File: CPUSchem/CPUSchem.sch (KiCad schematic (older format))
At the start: 30 parts

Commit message: Split CPU fetch stage into 2 stages to account for new interconnect
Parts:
- removed U?: IF_ID, symbol SOC:IF_ID
- added U?: IF1_IF2, symbol CPUSchem:IF1_IF2
- added U?: IF2_ID, symbol CPUSchem:IF2_ID
- U? (x10): symbol SOC:2-1Mux -> CPUSchem:2-1Mux
- U?: symbol SOC:MEM_WB -> CPUSchem:MEM_WB
- U?: symbol SOC:LOAD_UPPER -> CPUSchem:LOAD_UPPER
- U?: symbol SOC:3-1MUX -> CPUSchem:3-1MUX
- U? (x3): symbol SOC:ADDER -> CPUSchem:ADDER
- U?: symbol SOC:ID_IE -> CPUSchem:ID_IE
- U?: symbol SOC:IE_MEM -> CPUSchem:IE_MEM
- U?: symbol SOC:REGFILE -> CPUSchem:REGFILE
- U?: symbol SOC:IMM_GEN -> CPUSchem:IMM_GEN
- U?: symbol SOC:PC -> CPUSchem:PC
- U?: symbol SOC:DECODER -> CPUSchem:DECODER
- U?: symbol SOC:BRANCH_UNIT -> CPUSchem:BRANCH_UNIT
- U?: symbol SOC:HAZARD_UNIT -> CPUSchem:HAZARD_UNIT
- U?: symbol SOC:ALU -> CPUSchem:ALU
- U?: symbol SOC:DBUS_MASTER -> CPUSchem:DBUS_MASTER
- U?: symbol SOC:0Comparator -> CPUSchem:0Comparator
- U?: symbol SOC:FORWARDING_UNIT -> CPUSchem:FORWARDING_UNIT
- U?: symbol SOC:IBUS -> CPUSchem:IBUS
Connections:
- net labels added: Clr_F2, DBus_WaitReq_M, En_F2
- net labels removed: DBUS_WaitReq_M
- wire segments 135 -> 136
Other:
- note added: "Two Stage\nPipelined"

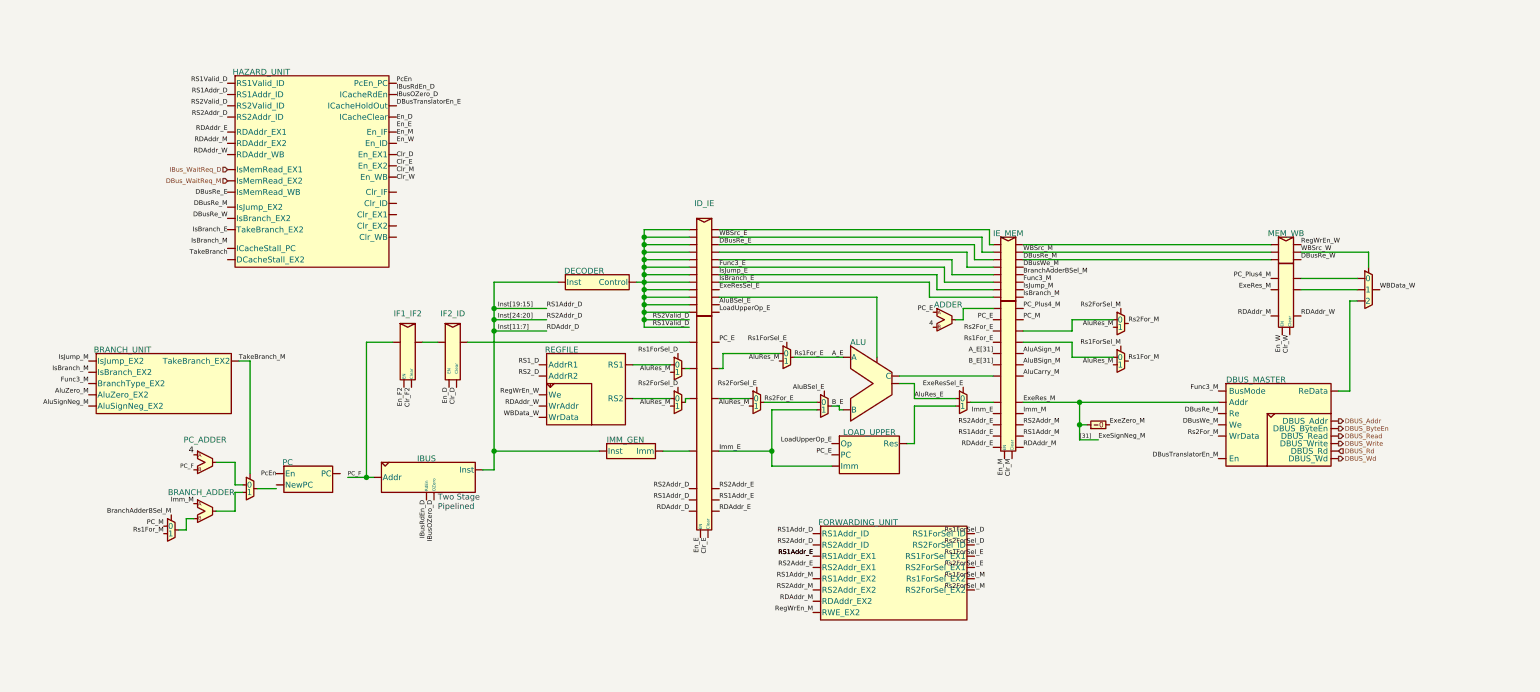
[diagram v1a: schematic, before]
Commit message: More CPU hazzard testing/fixes and verification
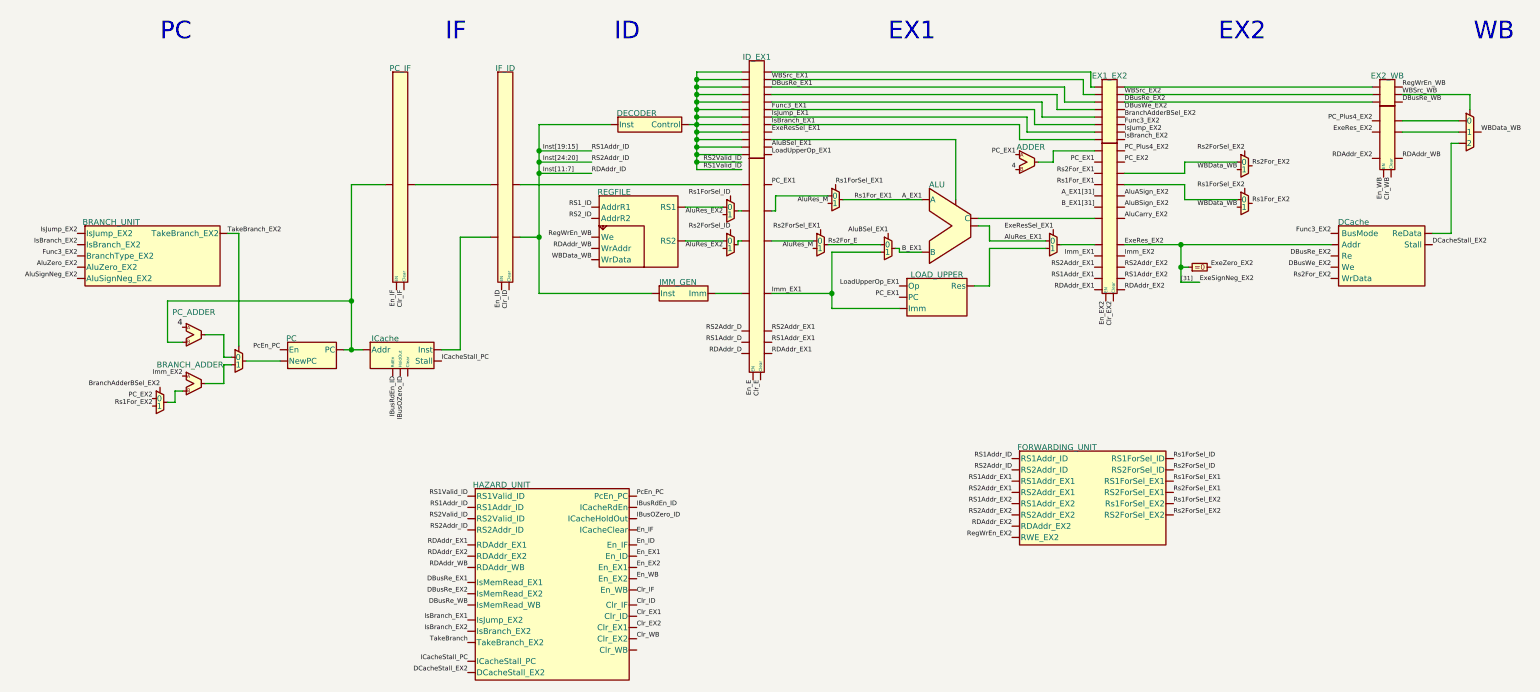
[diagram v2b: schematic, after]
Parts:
- removed U?: MEM_WB, symbol CPUSchem:MEM_WB
- removed U?: ID_IE, symbol CPUSchem:ID_IE
- removed U?: IE_MEM, symbol CPUSchem:IE_MEM
- removed U?: DBUS_MASTER, symbol CPUSchem:DBUS_MASTER
- removed U?: IBUS, symbol CPUSchem:IBUS
- removed U?: IF1_IF2, symbol CPUSchem:IF1_IF2
- removed U?: IF2_ID, symbol CPUSchem:IF2_ID
- added U?: PC_IF, symbol CPUSchem:PC_IF
- added U?: ICache, symbol CPUSchem:ICache
- added U?: IF_ID, symbol CPUSchem:IF_ID
- added U?: ID_EX1, symbol CPUSchem:ID_EX1
- added U?: EX1_EX2, symbol CPUSchem:EX1_EX2
- added U?: DCache, symbol CPUSchem:DCache
- added U?: EX2_WB, symbol CPUSchem:EX2_WB
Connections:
- net AluBSel_E is gone; now on net Rs2For_E: U?.~
- net AluSignNeg_M is gone; now on net TakeBranch_EX2: U?.~ (TakeBranch_EX2)
- net AluZero_M is gone; now on net TakeBranch_EX2: U?.~ (TakeBranch_EX2)
- net BranchAdderBSel_M is gone; now on net Rs1For_EX2: U?.~
- net DBusRe_M is gone; now on net TakeBranch: U?.~ (TakeBranch_EX2)
- net DBusRe_W is gone; now on net TakeBranch: U?.~ (TakeBranch_EX2)
- net DBusTranslatorEn_E is gone; now on net TakeBranch: U?.~ (TakeBranch_EX2)
- net DBus_WaitReq_M is gone; now on net TakeBranch: U?.~ (TakeBranch_EX2)
- net En_W is gone; now on net TakeBranch: U?.~ (TakeBranch_EX2)
- net ExeResSel_E is gone; now on net ExeResSel_EX1: U?.~
- net ExeZero_M is gone; now on net ExeZero_EX2: U?.~
- net Func3_M is gone; now on net TakeBranch_EX2: U?.~ (TakeBranch_EX2)
- net IBus_WaitReq_D is gone; now on net TakeBranch: U?.~ (TakeBranch_EX2)
- net Imm_M is gone; now on net Imm_EX2: U?.~
- net IsBranch_M is gone; now on net TakeBranch_EX2: U?.~ (TakeBranch_EX2)
- net IsJump_M is gone; now on net TakeBranch_EX2: U?.~ (TakeBranch_EX2)
- net LoadUpperOp_E is gone; now on net PC_EX1: U?.~ (Res)
- net PC_E is gone; now on net PC_EX1: U?.~, U?.~ (Res)
- net PC_F is gone; now on net 4: U?.~
- net PC_M is gone; now on net Rs1For_EX2: U?.~
- net PcEn is gone; now on net TakeBranch: U?.~ (TakeBranch_EX2)
- net RDAddr_E is gone; now on net TakeBranch: U?.~ (TakeBranch_EX2)
- net RS1Addr_E is gone; now on net Rs2ForSel_ID: U?.~ (RWE_EX2)
- net RS1Addr_M is gone; now on net Rs2ForSel_ID: U?.~ (RWE_EX2)
- net RS1_D is gone; now on net WBData_WB: U?.~ (WrData)
- net RS2Addr_E is gone; now on net Rs2ForSel_ID: U?.~ (RWE_EX2)
- net RS2Addr_M is gone; now on net Rs2ForSel_ID: U?.~ (RWE_EX2)
- net RS2_D is gone; now on net WBData_WB: U?.~ (WrData)
- net RegWrEn_M is gone; now on net Rs2ForSel_ID: U?.~ (RWE_EX2)
- net RegWrEn_W is gone; now on net WBData_WB: U?.~ (WrData)
- net Rs1ForSel_D is gone; now on net Rs1ForSel_ID: U?.~
- net Rs1ForSel_E is gone; now on net Rs1ForSel_EX1: U?.~
- net Rs1ForSel_M is gone; now on net WBData_WB: U?.~
- net Rs2ForSel_D is gone; now on net Rs2ForSel_ID: U?.~
- net Rs2ForSel_E is gone; now on net Rs2For_E: U?.~
- net Rs2ForSel_M is gone; now on net WBData_WB: U?.~
- net Rs2For_M is gone; now on net WBData_WB: U?.~
- net TakeBranch_M is gone; now on net TakeBranch_EX2: U?.~, U?.~ (TakeBranch_EX2)
- net WBSrc_W is gone; now on net WBSrc_WB: U?.~
- net AluRes_M: no longer U?.~, U?.~, U?.~, U?.~
- net Clr_E: now also U?.~; no longer U?.~ (TakeBranch_EX2)
- net En_E: now also U?.~
- net Inst[11:7]: now also U?.~
- net Rs1ForSel_EX1: now reaches U?.~
- net Rs1ForSel_EX1: now also U?.~ (RWE_EX2)
- net WBData_WB: now reaches U?.~
- net WBData_WB: now also U?.~
- net WBSrc_WB: now reaches U?.~
- net WBSrc_WB: now also U?.~
- net ExeResSel_EX1: now reaches U?.~
- net ExeResSel_EX1: now also U?.~; no longer U?.~ (Res)
- net PC_EX1: now reaches U?.~
- net PC_EX1: now also U?.~, U?.~
- net B_EX1: now reaches U?.~
- net B_EX1: now also U?.~
- net Rs1ForSel_ID: now reaches U?.~
- net Rs1ForSel_ID: now also U?.~ (RWE_EX2)
- net Rs2ForSel_ID: now reaches U?.~
- net PcEn_PC: now reaches U?.~ (PC)
- net PcEn_PC: now also U?.~ (TakeBranch_EX2)
- net TakeBranch_EX2: now reaches U?.~
- net TakeBranch_EX2: no longer U?.~
- net Imm_EX2: now reaches U?.~
- net Imm_EX2: now also U?.~; no longer U?.~
- net Rs1For_EX2: now reaches U?.~
- net Rs1For_EX2: now also U?.~; no longer U?.~
- removed net A_E: U?.~, U?.~
- removed net AluRes_E: U?.~, U?.~
- removed net B_E: U?.~, U?.~
- net ExeRes_M renamed ExeZero_EX2
- removed net Imm_E: U?.~, U?.~ (Res)
- removed net RDAddr_M: U?.~ (RWE_EX2), U?.~ (TakeBranch_EX2)
- removed net RDAddr_W: U?.~ (TakeBranch_EX2), U?.~ (WrData)
- net RS1Valid_D renamed RS1Valid_ID
- net RS1Valid_ID: now also U?.~
- removed net Rs1For_M: U?.~, U?.~
- removed net WBData_W: U?.~, U?.~ (WrData)
- new net: U?.~, U?.~ (x21)
- new net: U?.~, U?.~ (Res)
- new net: U?.~, U?.~ (WrData) (x3)
- new net: U?.~, U?.~ (Inst)
- new net: U?.~, U?.~, U?.~ (PC), U?.~ (Stall)
- new net: U?.~, U?.~ (PC)
- new net: U?.~, U?.~ (Stall)
- new net A_EX1: U?.~, U?.~, U?.~
- new net A_EX1[31]: U?.~
- new net AluASign_EX2: U?.~
- new net AluBSel_EX1: U?.~, U?.~
- new net AluBSign_EX2: U?.~
- new net AluCarry_EX2: U?.~
- new net AluRes_EX1: U?.~, U?.~
- new net AluRes_EX2: U?.~, U?.~
- new net AluSignNeg_EX2: U?.~ (TakeBranch_EX2)
- new net AluZero_EX2: U?.~ (TakeBranch_EX2)
- new net B_EX1[31]: U?.~
- new net BranchAdderBSel_EX2: U?.~, U?.~
- new net Clr_EX1: U?.~ (TakeBranch_EX2)
- new net Clr_EX2: U?.~, U?.~ (TakeBranch_EX2)
- new net Clr_ID: U?.~, U?.~ (TakeBranch_EX2)
- new net Clr_IF: U?.~
- new net Clr_WB: U?.~, U?.~ (TakeBranch_EX2)
- new net DBusRe_EX1: U?.~, U?.~, U?.~ (TakeBranch_EX2)
- new net DBusRe_EX2: U?.~, U?.~, U?.~ (TakeBranch_EX2), U?.~ (WrData)
- new net DBusRe_WB: U?.~, U?.~ (TakeBranch_EX2)
- new net DBusWe_EX2: U?.~, U?.~ (WrData)
- new net DCacheStall_EX2: U?.~ (TakeBranch_EX2), U?.~ (WrData)
- new net En_EX1: U?.~ (TakeBranch_EX2)
- new net En_EX2: U?.~, U?.~ (TakeBranch_EX2)
- new net En_ID: U?.~, U?.~ (TakeBranch_EX2)
- new net En_IF: U?.~
- new net En_WB: U?.~, U?.~ (TakeBranch_EX2)
- new net ExeRes_EX2: U?.~, U?.~, U?.~, U?.~ (WrData)
- new net Func3_EX1: U?.~, U?.~
- new net Func3_EX2: U?.~, U?.~ (TakeBranch_EX2), U?.~ (WrData)
- new net IBusOZero_ID: U?.~ (TakeBranch_EX2)
- new net IBusRdEn_ID: U?.~ (TakeBranch_EX2)
- new net ICacheStall_PC: U?.~ (Stall), U?.~ (TakeBranch_EX2)
- new net Imm_EX1: U?.~, U?.~, U?.~, U?.~ (Res)
- new net IsBranch_EX1: U?.~, U?.~, U?.~ (TakeBranch_EX2)
- new net IsBranch_EX2: U?.~, U?.~ (TakeBranch_EX2), U?.~ (TakeBranch_EX2)
- new net IsJump_EX1: U?.~, U?.~
- new net IsJump_EX2: U?.~, U?.~ (TakeBranch_EX2)
- new net LoadUpperOp_EX1: U?.~, U?.~ (Res)
- new net PC_EX2: U?.~, U?.~
- new net PC_Plus4_EX2: U?.~, U?.~
- new net RDAddr_D: U?.~
- new net RDAddr_EX1: U?.~, U?.~, U?.~ (TakeBranch_EX2)
- new net RDAddr_EX2: U?.~, U?.~, U?.~ (RWE_EX2), U?.~ (TakeBranch_EX2)
- new net RDAddr_WB: U?.~, U?.~ (TakeBranch_EX2), U?.~ (WrData)
- new net RS1Addr_D: U?.~
- new net RS1Addr_EX1: U?.~, U?.~, U?.~ (RWE_EX2)
- new net RS1Addr_EX2: U?.~, U?.~ (RWE_EX2)
- new net RS1_ID: U?.~ (WrData)
- new net RS2Addr_D: U?.~
- new net RS2Addr_EX1: U?.~, U?.~, U?.~ (RWE_EX2)
- new net RS2Addr_EX2: U?.~, U?.~ (RWE_EX2)
- new net RS2_ID: U?.~ (WrData)
- new net RegWrEn_EX2: U?.~ (RWE_EX2)
- new net RegWrEn_WB: U?.~, U?.~ (WrData)
- new net Rs1ForSel_EX2: U?.~, U?.~ (RWE_EX2)
- new net Rs2ForSel_EX1: U?.~, U?.~ (RWE_EX2)
- new net Rs2ForSel_EX2: U?.~, U?.~ (RWE_EX2)
- new net Rs2For_EX1: U?.~
- new net Rs2For_EX2: U?.~, U?.~ (WrData)
- new net WBSrc_EX1: U?.~, U?.~
- new net WBSrc_EX2: U?.~, U?.~
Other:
- note added: "EX1"
- note added: "EX2"
- note added: "ID"
- note added: "IF"
- note added: "PC"
- note added: "WB"
- note removed: "Two Stage\nPipelined"

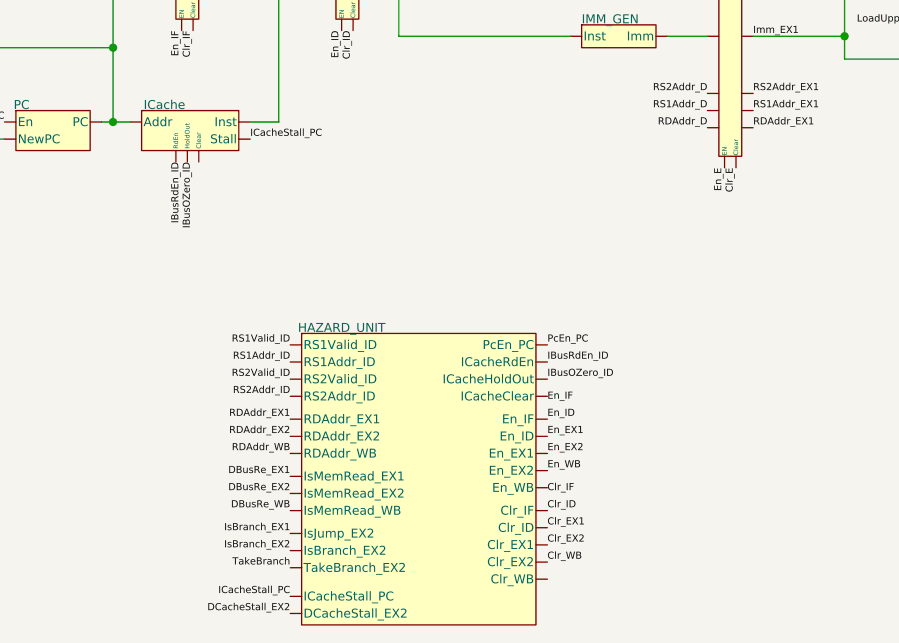
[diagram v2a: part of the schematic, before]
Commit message: Fixed branch hazzard bug
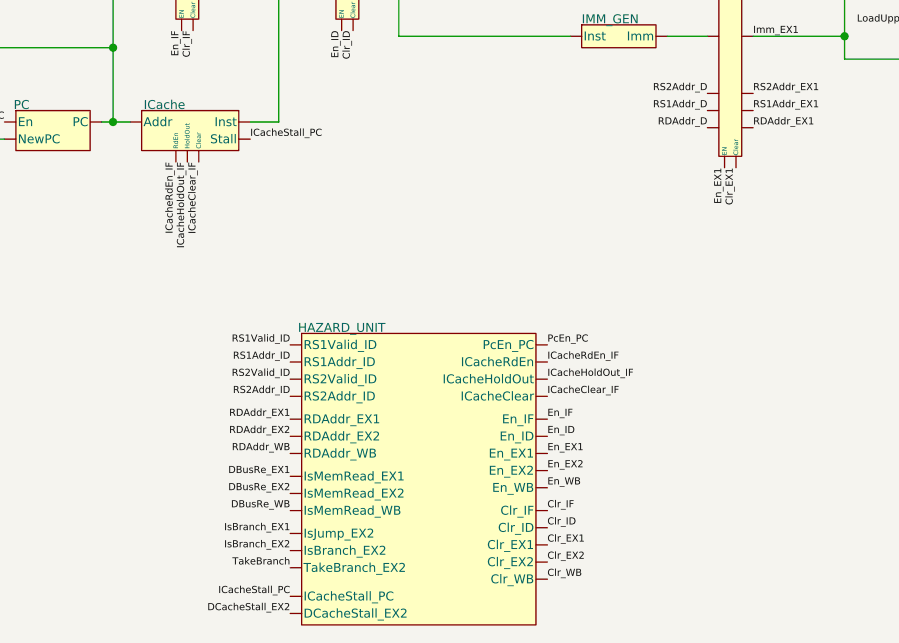
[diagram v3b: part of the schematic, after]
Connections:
- net Clr_E is gone; now on net WBSrc_EX1: U?.~
- net En_E is gone; now on net WBSrc_EX1: U?.~
- net IBusOZero_ID is gone; now on net TakeBranch: U?.~ (TakeBranch_EX2)
- net IBusRdEn_ID is gone; now on net TakeBranch: U?.~ (TakeBranch_EX2)
- net Clr_EX1: now also U?.~
- net Clr_IF: now also U?.~ (TakeBranch_EX2)
- net En_EX1: now also U?.~
- net En_IF: now also U?.~ (TakeBranch_EX2)
- new net: U?.~, U?.~ (x21)
- new net: U?.~, U?.~ (Res)
- new net: U?.~, U?.~ (WrData) (x3)
- new net: U?.~, U?.~ (Inst)
- new net: U?.~, U?.~, U?.~ (PC), U?.~ (Stall)
- new net: U?.~, U?.~ (PC)
- new net: U?.~, U?.~ (Stall)
- new net ICacheClear_IF: U?.~ (Stall), U?.~ (TakeBranch_EX2)
- new net ICacheHoldOut_IF: U?.~ (Stall), U?.~ (TakeBranch_EX2)
- new net ICacheRdEn_IF: U?.~ (Stall), U?.~ (TakeBranch_EX2)
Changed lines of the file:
@@
 EESchema Schematic File Version 4
-LIBS:CPUSchem-cache
 EELAYER 30 0
 EELAYER END
@@
 	5325 1800 5625 1800
 Text Label 5700 3350 3    31   ~ 0
-En_E
+En_EX1
 Text Label 5750 3350 3    31   ~ 0
-Clr_E
+Clr_EX1
 Text Label 5825 2050 0    31   ~ 0
 PC_EX1
@@
 Text Label 3800 5100 2    31   ~ 0
 TakeBranch
+Text Label 4925 4600 0    31   ~ 0
+En_EX1
+Text Label 4925 5000 0    31   ~ 0
+Clr_EX1
 Text Label 4925 4525 0    31   ~ 0
-En_EX1
+En_ID
 Text Label 4925 4925 0    31   ~ 0
-Clr_EX1
-Text Label 4925 4450 0    31   ~ 0
-En_ID
-Text Label 4925 4850 0    31   ~ 0
 Clr_ID
-Text Label 4925 4600 0    31   ~ 0
+Text Label 4925 4675 0    31   ~ 0
 En_EX2
-Text Label 4925 5000 0    31   ~ 0
+Text Label 4925 5075 0    31   ~ 0
 Clr_EX2
 Text Label 2550 3150 2    31   ~ 0
@@
 	3100 3150 3025 3150
 Text Label 4925 4200 0    31   ~ 0
-IBusRdEn_ID
-Text Label 4925 4275 0    31   ~ 0
-IBusOZero_ID
+ICacheRdEn_IF
 $Comp
 L CPUSchem:ADDER U?
@@
 	5325 1350 5325 1400
 Connection ~ 5325 1400
-Text Label 4925 5075 0    31   ~ 0
+Text Label 4925 5150 0    31   ~ 0
 Clr_WB
-Text Label 4925 4675 0    31   ~ 0
+Text Label 4925 4750 0    31   ~ 0
 En_WB
 Text Label 8500 4250 0    31   ~ 0
@@
 Text Label 5825 1700 0    31   ~ 0
 ExeResSel_EX1
-Text Label 3325 3325 3    31   ~ 0
-IBusRdEn_ID
-Text Label 3375 3325 3    31   ~ 0
-IBusOZero_ID
 Wire Wire Line
 	5825 1750 7050 1750
@@
 	1    0    0    -1
 $EndComp
-$Comp
-L CPUSchem:ICache U?
-U 1 1 5FED08D9
-P 3300 3175
-F 0 "U?" H 3025 3400 50  0001 C CNN
-F 1 "ICache" H 3250 3275 39  0000 C CNN
-F 2 "" H 2975 3325 50  0001 C CNN
-F 3 "" H 2975 3325 50  0001 C CNN
-	1    3300 3175
-	1    0    0    -1
-$EndComp
 Text Notes 4775 1100 0    118  ~ 0
 ID
@@
 Text Label 4075 2750 3    31   ~ 0
 Clr_ID
-Text Label 4925 4375 0    31   ~ 0
+Text Label 4925 4450 0    31   ~ 0
 En_IF
-Text Label 4925 4775 0    31   ~ 0
+Text Label 4925 4850 0    31   ~ 0
 Clr_IF
 Wire Wire Line
@@
 	1    0    0    -1
 $EndComp
-Text Label 8050 2825 3    31   ~ 0
-En_EX2
 Text Label 8100 2825 3    31   ~ 0
 Clr_EX2
@@
 Text Label 8925 2200 2    31   ~ 0
 WBData_WB
+Text Label 4925 4275 0    31   ~ 0
+ICacheHoldOut_IF
+Text Label 4925 4350 0    31   ~ 0
+ICacheClear_IF
+Text Label 3400 3325 3    31   ~ 0
+ICacheClear_IF
+Text Label 3350 3325 3    31   ~ 0
+ICacheHoldOut_IF
+Text Label 3300 3325 3    31   ~ 0
+ICacheRdEn_IF
+$Comp
+L CPUSchem:ICache U?
+U 1 1 5FED08D9
+P 3300 3175
+F 0 "U?" H 3025 3400 50  0001 C CNN
+F 1 "ICache" H 3250 3275 39  0000 C CNN
+F 2 "" H 2975 3325 50  0001 C CNN
+F 3 "" H 2975 3325 50  0001 C CNN
+	1    3300 3175
+	1    0    0    -1
+$EndComp
+Text Label 8050 2825 3    31   ~ 0
+En_EX2
 $EndSCHEMATC
